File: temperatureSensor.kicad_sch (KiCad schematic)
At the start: 1 part, among them IC2 LMT87LPG

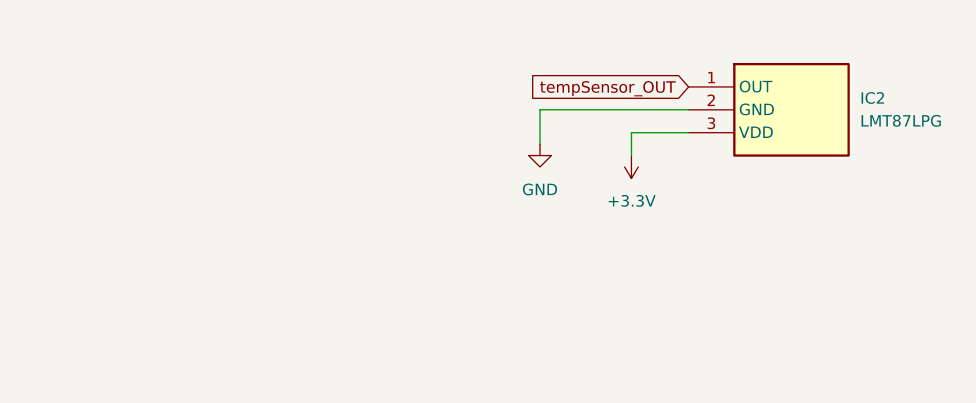
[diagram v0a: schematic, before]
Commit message: updated temperature sensor
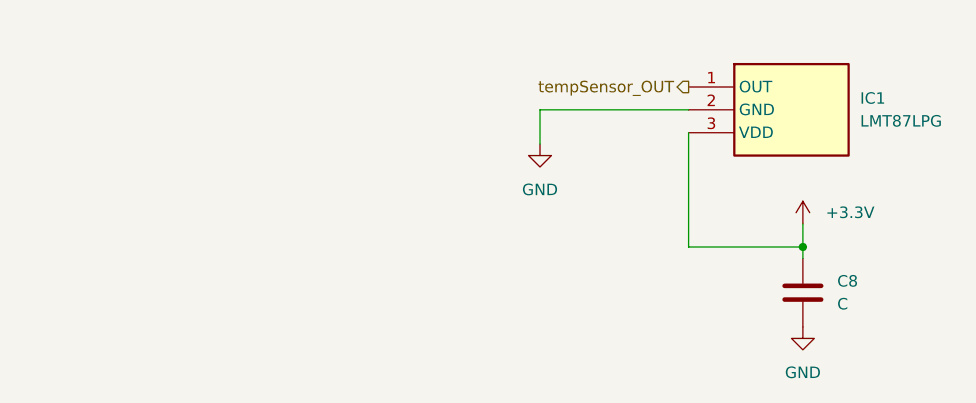
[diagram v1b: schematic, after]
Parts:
- added C8: C, symbol Device:C
- renumbered IC2 to IC1
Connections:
- net +3.3V: now also C8.1
- net GND: now also C8.2
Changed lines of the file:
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@@
 (kicad_sch (version 20230121) (generator eeschema)
   (paper "A4")
-  (wire (pts (xy 91.44 82.55) (xy 91.44 80.01))
-    (stroke (width 0) (type default))
+  (junction (at 110.49 92.71) (diameter 0) (color 0 0 0 0)
   )
-  (wire (pts (xy 91.44 80.01) (xy 97.79 80.01))
+  (wire (pts (xy 110.49 92.71) (xy 110.49 93.98))
     (stroke (width 0) (type default))
   )
@@
     (stroke (width 0) (type default))
   )
+  (wire (pts (xy 110.49 90.17) (xy 110.49 92.71))
+    (stroke (width 0) (type default))
+  )
+  (wire (pts (xy 97.79 92.71) (xy 110.49 92.71))
+    (stroke (width 0) (type default))
+  )
+  (wire (pts (xy 97.79 80.01) (xy 97.79 92.71))
+    (stroke (width 0) (type default))
+  )
   (wire (pts (xy 81.28 77.47) (xy 81.28 81.28))
     (stroke (width 0) (type default))
   )
-  (global_label "tempSensor_OUT" (shape input) (at 97.79 74.93 180) (fields_autoplaced)
+  (hierarchical_label "tempSensor_OUT" (shape output) (at 97.79 74.93 180) (fields_autoplaced)
     (effects (font (size 1.27 1.27)) (justify right))
-    (property "Intersheetrefs" "${INTERSHEET_REFS}" (at 79.1416 74.93 0)
-      (effects (font (size 1.27 1.27)) (justify right) hide)
+  )
+  (symbol (lib_id "Device:C") (at 110.49 97.79 0) (unit 1)
+    (in_bom yes) (on_board yes) (dnp no) (fields_autoplaced)
+    (property "Reference" "C8" (at 114.3 96.52 0)
+      (effects (font (size 1.27 1.27)) (justify left))
+    )
+    (property "Value" "C" (at 114.3 99.06 0)
+      (effects (font (size 1.27 1.27)) (justify left))
+    )
+    (property "Footprint" "" (at 111.4552 101.6 0)
+      (effects (font (size 1.27 1.27)) hide)
+    )
+    (property "Datasheet" "~" (at 110.49 97.79 0)
+      (effects (font (size 1.27 1.27)) hide)
+    )
+    (pin "1")
+    (pin "2")
+    (instances
+      (project "Telemetry-Peripheral-SOM-Daughterboard-IMU"
+        (path "/637f68f0-cb9c-412a-8573-5d8e7ef6d8a2/0366cb5e-31c7-40b1-9d0c-97ad688b48f0"
+          (reference "C8") (unit 1)
+        )
+      )
     )
   )
-  (symbol (lib_id "power:+3.3V") (at 91.44 82.55 180) (unit 1)
+  (symbol (lib_id "power:GND") (at 110.49 101.6 0) (unit 1)
     (in_bom yes) (on_board yes) (dnp no) (fields_autoplaced)
-    (property "Reference" "#PWR016" (at 91.44 78.74 0)
+    (property "Reference" "#PWR018" (at 110.49 107.95 0)
       (effects (font (size 1.27 1.27)) hide)
     )
-    (property "Value" "+3.3V" (at 91.44 87.63 0)
+    (property "Value" "GND" (at 110.49 106.68 0)
       (effects (font (size 1.27 1.27)))
     )
-    (property "Footprint" "" (at 91.44 82.55 0)
+    (property "Footprint" "" (at 110.49 101.6 0)
       (effects (font (size 1.27 1.27)) hide)
     )
-    (property "Datasheet" "" (at 91.44 82.55 0)
+    (property "Datasheet" "" (at 110.49 101.6 0)
+      (effects (font (size 1.27 1.27)) hide)
+    )
+    (pin "1")
+    (instances
+      (project "Telemetry-Peripheral-SOM-Daughterboard-IMU"
+        (path "/637f68f0-cb9c-412a-8573-5d8e7ef6d8a2/0366cb5e-31c7-40b1-9d0c-97ad688b48f0"
+          (reference "#PWR018") (unit 1)
+        )
+      )
+    )
+  )
+  (symbol (lib_id "power:+3.3V") (at 110.49 90.17 0) (unit 1)
+    (in_bom yes) (on_board yes) (dnp no) (fields_autoplaced)
+    (property "Reference" "#PWR016" (at 110.49 93.98 0)
+      (effects (font (size 1.27 1.27)) hide)
+    )
+    (property "Value" "+3.3V" (at 113.03 88.9 0)
+      (effects (font (size 1.27 1.27)) (justify left))
+    )
+    (property "Footprint" "" (at 110.49 90.17 0)
+      (effects (font (size 1.27 1.27)) hide)
+    )
+    (property "Datasheet" "" (at 110.49 90.17 0)
       (effects (font (size 1.27 1.27)) hide)
     )
@@
   (symbol (lib_id "utsvt-chips:LMT87LPG") (at 97.79 74.93 0) (unit 1)
     (in_bom yes) (on_board yes) (dnp no) (fields_autoplaced)
-    (property "Reference" "IC2" (at 116.84 76.2 0)
+    (property "Reference" "IC1" (at 116.84 76.2 0)
       (effects (font (size 1.27 1.27)) (justify left))
     )
@@
       (project "Telemetry-Peripheral-SOM-Daughterboard-IMU"
         (path "/637f68f0-cb9c-412a-8573-5d8e7ef6d8a2/0366cb5e-31c7-40b1-9d0c-97ad688b48f0"
-          (reference "IC2") (unit 1)
+          (reference "IC1") (unit 1)
         )
       )

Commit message: temperatureSensor fix
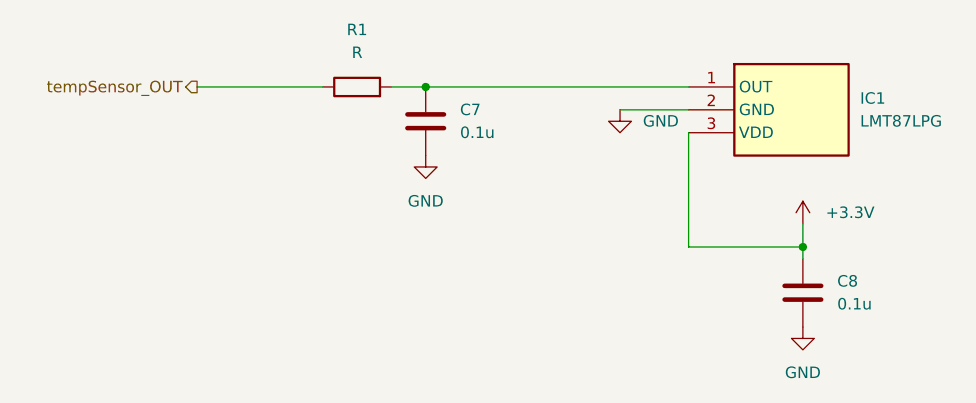
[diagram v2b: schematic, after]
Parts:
- added C7: 0.1u, symbol Device:C
- added R1: R, symbol Device:R
- C8: value C -> 0.1u
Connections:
- net GND: now also C7.2
- net tempSensor_OUT: now also R1.1; no longer IC1.1 (OUT)
- new net: C7.1, IC1.1 (OUT), R1.2
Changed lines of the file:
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@@
 (kicad_sch (version 20230121) (generator eeschema)
   (paper "A4")
+  (junction (at 68.58 74.93) (diameter 0) (color 0 0 0 0)
+  )
   (junction (at 110.49 92.71) (diameter 0) (color 0 0 0 0)
+  )
+  (wire (pts (xy 43.18 74.93) (xy 57.15 74.93))
+    (stroke (width 0) (type default))
   )
   (wire (pts (xy 110.49 92.71) (xy 110.49 93.98))
     (stroke (width 0) (type default))
   )
-  (wire (pts (xy 97.79 77.47) (xy 81.28 77.47))
+  (wire (pts (xy 90.17 77.47) (xy 97.79 77.47))
+    (stroke (width 0) (type default))
+  )
+  (wire (pts (xy 68.58 74.93) (xy 97.79 74.93))
     (stroke (width 0) (type default))
   )
@@
     (stroke (width 0) (type default))
   )
-  (wire (pts (xy 81.28 77.47) (xy 81.28 81.28))
+  (wire (pts (xy 64.77 74.93) (xy 68.58 74.93))
     (stroke (width 0) (type default))
   )
-  (hierarchical_label "tempSensor_OUT" (shape output) (at 97.79 74.93 180) (fields_autoplaced)
+  (hierarchical_label "tempSensor_OUT" (shape output) (at 43.18 74.93 180) (fields_autoplaced)
     (effects (font (size 1.27 1.27)) (justify right))
+  )
+  (symbol (lib_id "Device:R") (at 60.96 74.93 90) (unit 1)
+    (in_bom yes) (on_board yes) (dnp no) (fields_autoplaced)
+    (property "Reference" "R1" (at 60.96 68.58 90)
+      (effects (font (size 1.27 1.27)))
+    )
+    (property "Value" "R" (at 60.96 71.12 90)
+      (effects (font (size 1.27 1.27)))
+    )
+    (property "Footprint" "" (at 60.96 76.708 90)
+      (effects (font (size 1.27 1.27)) hide)
+    )
+    (property "Datasheet" "~" (at 60.96 74.93 0)
+      (effects (font (size 1.27 1.27)) hide)
+    )
+    (pin "1")
+    (pin "2")
+    (instances
+      (project "Telemetry-Peripheral-SOM-Daughterboard-IMU"
+        (path "/637f68f0-cb9c-412a-8573-5d8e7ef6d8a2/0366cb5e-31c7-40b1-9d0c-97ad688b48f0"
+          (reference "R1") (unit 1)
+        )
+      )
+    )
   )
   (symbol (lib_id "Device:C") (at 110.49 97.79 0) (unit 1)
@@
       (effects (font (size 1.27 1.27)) (justify left))
     )
-    (property "Value" "C" (at 114.3 99.06 0)
+    (property "Value" "0.1u" (at 114.3 99.06 0)
       (effects (font (size 1.27 1.27)) (justify left))
     )
@@
     )
   )
+  (symbol (lib_id "Device:C") (at 68.58 78.74 0) (unit 1)
+    (in_bom yes) (on_board yes) (dnp no) (fields_autoplaced)
+    (property "Reference" "C7" (at 72.39 77.47 0)
+      (effects (font (size 1.27 1.27)) (justify left))
+    )
+    (property "Value" "0.1u" (at 72.39 80.01 0)
+      (effects (font (size 1.27 1.27)) (justify left))
+    )
+    (property "Footprint" "" (at 69.5452 82.55 0)
+      (effects (font (size 1.27 1.27)) hide)
+    )
+    (property "Datasheet" "~" (at 68.58 78.74 0)
+      (effects (font (size 1.27 1.27)) hide)
+    )
+    (pin "1")
+    (pin "2")
+    (instances
+      (project "Telemetry-Peripheral-SOM-Daughterboard-IMU"
+        (path "/637f68f0-cb9c-412a-8573-5d8e7ef6d8a2/0366cb5e-31c7-40b1-9d0c-97ad688b48f0"
+          (reference "C7") (unit 1)
+        )
+      )
+    )
+  )
+  (symbol (lib_id "power:GND") (at 68.58 82.55 0) (unit 1)
+    (in_bom yes) (on_board yes) (dnp no) (fields_autoplaced)
+    (property "Reference" "#PWR017" (at 68.58 88.9 0)
+      (effects (font (size 1.27 1.27)) hide)
+    )
+    (property "Value" "GND" (at 68.58 87.63 0)
+      (effects (font (size 1.27 1.27)))
+    )
+    (property "Footprint" "" (at 68.58 82.55 0)
+      (effects (font (size 1.27 1.27)) hide)
+    )
+    (property "Datasheet" "" (at 68.58 82.55 0)
+      (effects (font (size 1.27 1.27)) hide)
+    )
+    (pin "1")
+    (instances
+      (project "Telemetry-Peripheral-SOM-Daughterboard-IMU"
+        (path "/637f68f0-cb9c-412a-8573-5d8e7ef6d8a2/0366cb5e-31c7-40b1-9d0c-97ad688b48f0"
+          (reference "#PWR017") (unit 1)
+        )
+      )
+    )
+  )
   (symbol (lib_id "power:+3.3V") (at 110.49 90.17 0) (unit 1)
     (in_bom yes) (on_board yes) (dnp no) (fields_autoplaced)
@@
     )
   )
-  (symbol (lib_id "power:GND") (at 81.28 81.28 0) (unit 1)
+  (symbol (lib_id "power:GND") (at 90.17 77.47 0) (unit 1)
     (in_bom yes) (on_board yes) (dnp no) (fields_autoplaced)
-    (property "Reference" "#PWR015" (at 81.28 87.63 0)
+    (property "Reference" "#PWR015" (at 90.17 83.82 0)
       (effects (font (size 1.27 1.27)) hide)
     )
-    (property "Value" "GND" (at 81.28 86.36 0)
-      (effects (font (size 1.27 1.27)))
+    (property "Value" "GND" (at 92.71 78.74 0)
+      (effects (font (size 1.27 1.27)) (justify left))
     )
-    (property "Footprint" "" (at 81.28 81.28 0)
+    (property "Footprint" "" (at 90.17 77.47 0)
       (effects (font (size 1.27 1.27)) hide)
     )
-    (property "Datasheet" "" (at 81.28 81.28 0)
+    (property "Datasheet" "" (at 90.17 77.47 0)
       (effects (font (size 1.27 1.27)) hide)
     )

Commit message: connected airflow and temperature sensors to connector J1
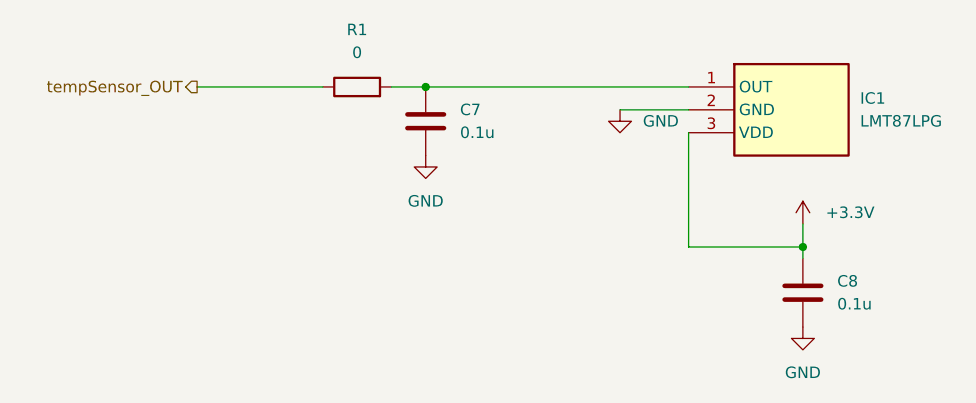
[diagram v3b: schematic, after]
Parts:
- R1: value R -> 0
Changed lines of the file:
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@@
       (effects (font (size 1.27 1.27)))
     )
-    (property "Value" "R" (at 60.96 71.12 90)
+    (property "Value" "0" (at 60.96 71.12 90)
       (effects (font (size 1.27 1.27)))
     )

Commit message: temp sensor library fix
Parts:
- IC1: footprint LMT87LPG -> UTSVT_ICs:LMT87LPG
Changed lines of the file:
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@@
       (effects (font (size 1.27 1.27)) (justify left))
     )
-    (property "Footprint" "LMT87LPG" (at 116.84 169.85 0)
+    (property "Footprint" "UTSVT_ICs:LMT87LPG" (at 116.84 169.85 0)
       (effects (font (size 1.27 1.27)) (justify left top) hide)
     )
